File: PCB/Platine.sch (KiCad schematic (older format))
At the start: 4 parts

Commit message: ESP Beschaltung fertig
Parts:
- added C1: 100nF, symbol C
- added R1, R2, R3, R4, R5: 10kR, symbol R
- added SW1: Reset, symbol SW_Push
- added SW2: Flash, symbol SW_Push
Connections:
- net RX: now also U?.15 (RXD)
- net TX: now also U?.16 (TXD)
- net at U?.1 (REST): now also R1.2, SW1.1
- net at U?.10 (GPIO15): now also R5.1
- net at U?.11 (GPIO2): now also R4.2
- net at U?.12 (GPIO0): now also R3.2, SW2.1
- net OnOff: now reaches U?.13 (GPIO4)
- net Servo: now reaches U?.14 (GPIO5)
- net at U?.3 (CH_PD): now also R2.2
- net LED_R: now reaches U?.4 (GPIO16)
- net LED_G: now reaches U?.5 (GPIO14)
- net LED_B: now reaches U?.6 (GPIO12)
- net +3V3: now reaches U?.8 (VCC)
- net +3V3: now also C1.1, R1.1, R2.1, R3.1, R4.1
- net GND: now reaches U?.9 (GND)
- net GND: now also C1.2, R5.2, SW1.2, SW2.2
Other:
- moved on the sheet: SW?, U?

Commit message: ESC
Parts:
- removed SW?: SW_Push, symbol SW_Push
- removed U?: LM2575, symbol LM2575
- added U?: AP2204K-3.3, TO_SOT_Packages_SMD:SOT-23-5, symbol AP2204K-3.3
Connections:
- net PWM_ESC: now reaches U?.7 (GPIO13)

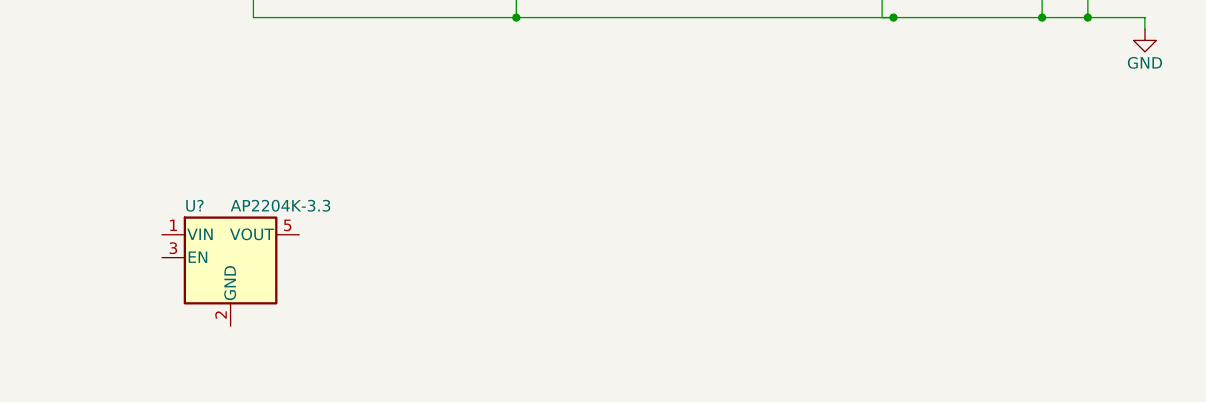
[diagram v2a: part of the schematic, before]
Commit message: added linreg
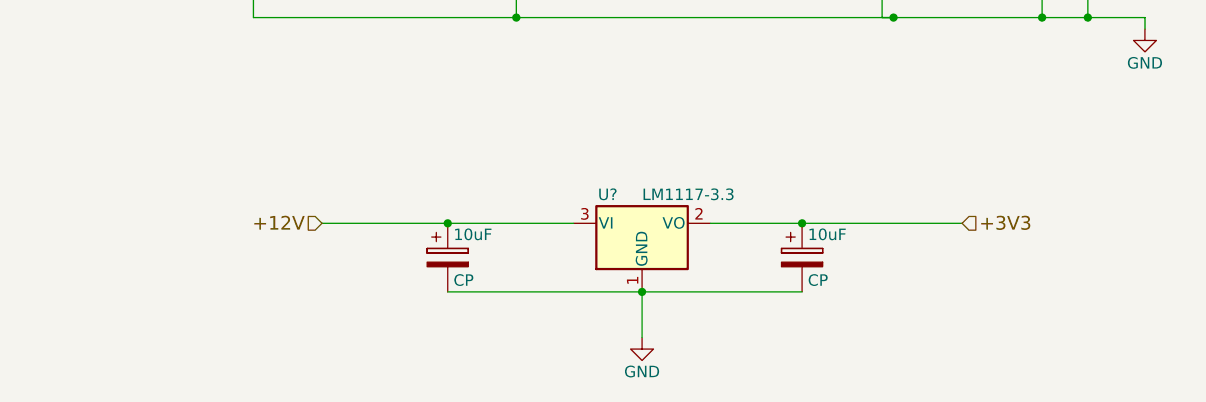
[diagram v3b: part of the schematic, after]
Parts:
- removed U?: AP2204K-3.3, TO_SOT_Packages_SMD:SOT-23-5, symbol AP2204K-3.3
- added 10uF (x2): CP, symbol CP
- added U?: LM1117-3.3, symbol LM1117-3.3
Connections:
- net +12V: now also 10uF.1, U?.3 (VI)
- net +3V3: now also 10uF.1, U?.2 (VO)
- net GND: now also 10uF.2, 10uF.2, U?.1 (GND)
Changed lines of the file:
@@
 Connection ~ 2900 4550
 $Comp
-L AP2204K-3.3 U?
-U 1 1 5BB4D2C1
-P 2800 6150
-F 0 "U?" H 2600 6375 50  0000 L CNN
-F 1 "AP2204K-3.3" H 2800 6375 50  0000 L CNN
-F 2 "TO_SOT_Packages_SMD:SOT-23-5" H 2800 6475 50  0001 C CNN
-F 3 "" H 2800 6250 50  0001 C CNN
-	1    2800 6150
+L LM1117-3.3 U?
+U 1 1 5BBE439C
+P 4600 6000
+F 0 "U?" H 4450 6125 50  0000 C CNN
+F 1 "LM1117-3.3" H 4600 6125 50  0000 L CNN
+F 2 "" H 4600 6000 50  0001 C CNN
+F 3 "" H 4600 6000 50  0001 C CNN
+	1    4600 6000
 	1    0    0    -1
 $EndComp
+$Comp
+L CP 10uF
+U 1 1 5BBE48BE
+P 3750 6150
+F 0 "10uF" H 3775 6250 50  0000 L CNN
+F 1 "CP" H 3775 6050 50  0000 L CNN
+F 2 "" H 3788 6000 50  0001 C CNN
+F 3 "" H 3750 6150 50  0001 C CNN
+	1    3750 6150
+	1    0    0    -1
+$EndComp
+$Comp
+L CP 10uF
+U 1 1 5BBE490E
+P 5300 6150
+F 0 "10uF" H 5325 6250 50  0000 L CNN
+F 1 "CP" H 5325 6050 50  0000 L CNN
+F 2 "" H 5338 6000 50  0001 C CNN
+F 3 "" H 5300 6150 50  0001 C CNN
+	1    5300 6150
+	1    0    0    -1
+$EndComp
+Wire Wire Line
+	3200 6000 4300 6000
+Wire Wire Line
+	4900 6000 6000 6000
+Wire Wire Line
+	3750 6300 5300 6300
+Connection ~ 4600 6300
+Text HLabel 6000 6000 2    60   Input ~ 0
++3V3
+Text HLabel 3200 6000 0    60   Input ~ 0
++12V
+Connection ~ 3750 6000
+Connection ~ 5300 6000
+$Comp
+L GND #PWR?
+U 1 1 5BBE52A5
+P 4600 6500
+F 0 "#PWR?" H 4600 6250 50  0001 C CNN
+F 1 "GND" H 4600 6350 50  0000 C CNN
+F 2 "" H 4600 6500 50  0001 C CNN
+F 3 "" H 4600 6500 50  0001 C CNN
+	1    4600 6500
+	1    0    0    -1
+$EndComp
+Wire Wire Line
+	4600 6500 4600 6300
 $EndSCHEMATC

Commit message: new code
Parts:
- U1: renamed from U?; footprint (none) -> TO_SOT_Packages_SMD:SOT-223
- U2: renamed from U?; footprint (none) -> RF_Modules:ESP-12E
- gave numbers to parts that had none: 1
- renumbered 10uF to 10uF1, 10uF to 10uF2
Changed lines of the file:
@@
 $EndDescr
 $Comp
-L ESP-12E U?
+L ESP-12E U2
 U 1 1 5BA69592
 P 4750 3700
-F 0 "U?" H 4750 3600 50  0000 C CNN
+F 0 "U2" H 4750 3600 50  0000 C CNN
 F 1 "ESP-12E" H 4750 3800 50  0000 C CNN
-F 2 "" H 4750 3700 50  0001 C CNN
+F 2 "RF_Modules:ESP-12E" H 4750 3700 50  0001 C CNN
 F 3 "" H 4750 3700 50  0001 C CNN
 	1    4750 3700
@@
 $EndComp
 $Comp
-L +12V #PWR?
+L +12V #PWR1
 U 1 1 5BA696C6
 P 1200 1000
-F 0 "#PWR?" H 1200 850 50  0001 C CNN
+F 0 "#PWR1" H 1200 850 50  0001 C CNN
 F 1 "+12V" H 1200 1140 50  0000 C CNN
 F 2 "" H 1200 1000 50  0001 C CNN
@@
 $EndComp
 $Comp
-L LED_CRGB D?
+L LED_CRGB D1
 U 1 1 5BA69725
 P 1850 3800
-F 0 "D?" H 1850 4170 50  0000 C CNN
+F 0 "D1" H 1850 4170 50  0000 C CNN
 F 1 "LED_CRGB" H 1850 3450 50  0000 C CNN
 F 2 "" H 1850 3750 50  0001 C CNN
@@
 GNDprg
 $Comp
-L +3V3 #PWR?
+L +3V3 #PWR2
 U 1 1 5BA79CF4
 P 2550 2750
-F 0 "#PWR?" H 2550 2600 50  0001 C CNN
+F 0 "#PWR2" H 2550 2600 50  0001 C CNN
 F 1 "+3V3" H 2550 2890 50  0000 C CNN
 F 2 "" H 2550 2750 50  0001 C CNN
@@
 $EndComp
 $Comp
-L GND #PWR?
+L GND #PWR4
 U 1 1 5BA79D10
 P 6800 5150
-F 0 "#PWR?" H 6800 4900 50  0001 C CNN
+F 0 "#PWR4" H 6800 4900 50  0001 C CNN
 F 1 "GND" H 6800 5000 50  0000 C CNN
 F 2 "" H 6800 5150 50  0001 C CNN
@@
 Connection ~ 2900 4550
 $Comp
-L LM1117-3.3 U?
+L LM1117-3.3 U1
 U 1 1 5BBE439C
 P 4600 6000
-F 0 "U?" H 4450 6125 50  0000 C CNN
+F 0 "U1" H 4450 6125 50  0000 C CNN
 F 1 "LM1117-3.3" H 4600 6125 50  0000 L CNN
-F 2 "" H 4600 6000 50  0001 C CNN
+F 2 "TO_SOT_Packages_SMD:SOT-223" H 4600 6000 50  0001 C CNN
 F 3 "" H 4600 6000 50  0001 C CNN
 	1    4600 6000
@@
 $EndComp
 $Comp
-L CP 10uF
+L CP 10uF1
 U 1 1 5BBE48BE
 P 3750 6150
-F 0 "10uF" H 3775 6250 50  0000 L CNN
+F 0 "10uF1" H 3775 6250 50  0000 L CNN
 F 1 "CP" H 3775 6050 50  0000 L CNN
 F 2 "" H 3788 6000 50  0001 C CNN
@@
 $EndComp
 $Comp
-L CP 10uF
+L CP 10uF2
 U 1 1 5BBE490E
 P 5300 6150
-F 0 "10uF" H 5325 6250 50  0000 L CNN
+F 0 "10uF2" H 5325 6250 50  0000 L CNN
 F 1 "CP" H 5325 6050 50  0000 L CNN
 F 2 "" H 5338 6000 50  0001 C CNN
@@
 Connection ~ 5300 6000
 $Comp
-L GND #PWR?
+L GND #PWR3
 U 1 1 5BBE52A5
 P 4600 6500
-F 0 "#PWR?" H 4600 6250 50  0001 C CNN
+F 0 "#PWR3" H 4600 6250 50  0001 C CNN
 F 1 "GND" H 4600 6350 50  0000 C CNN
 F 2 "" H 4600 6500 50  0001 C CNN
